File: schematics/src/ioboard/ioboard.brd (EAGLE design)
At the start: 160 x 98.7 mm, 31 parts

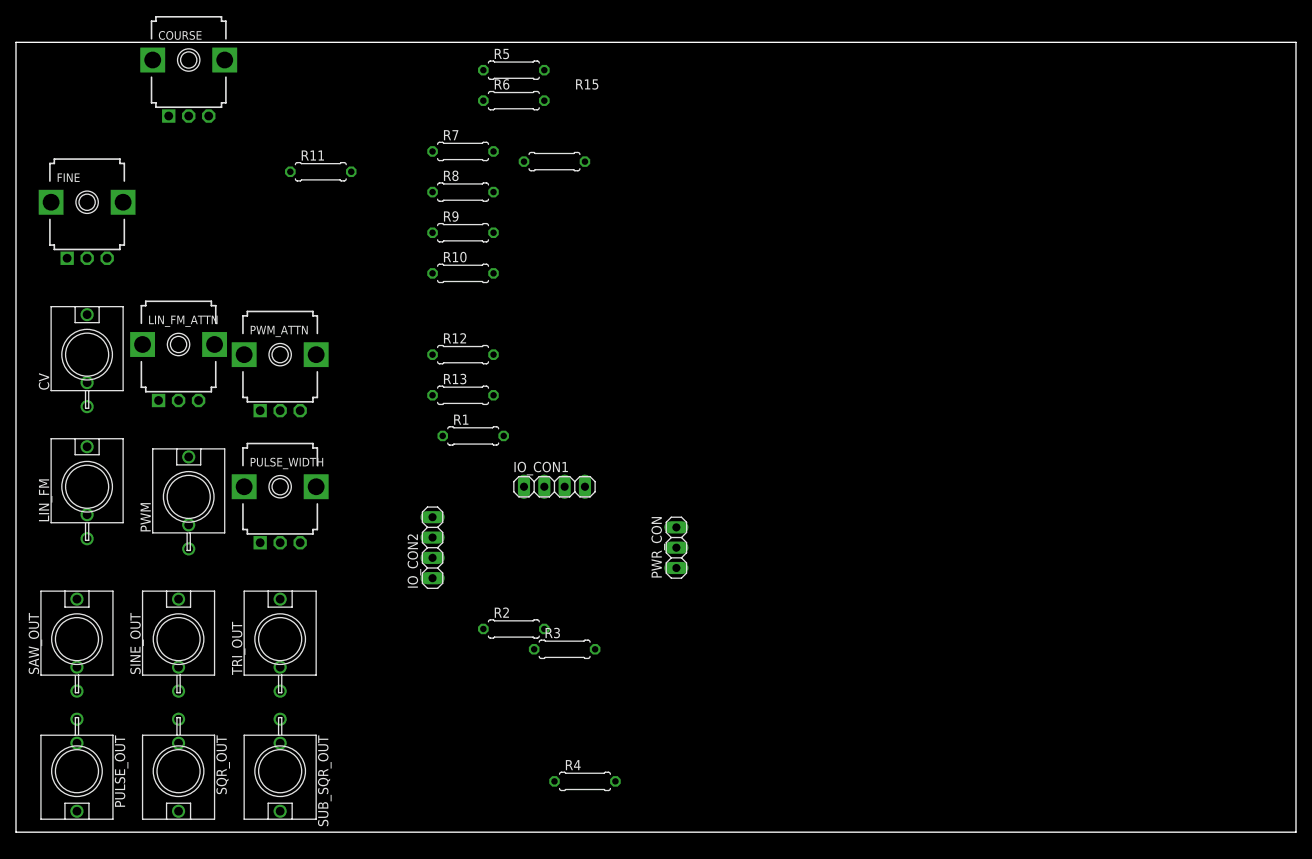
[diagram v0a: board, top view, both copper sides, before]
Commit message: Updated Schematics, Fixed Power Socket orientation
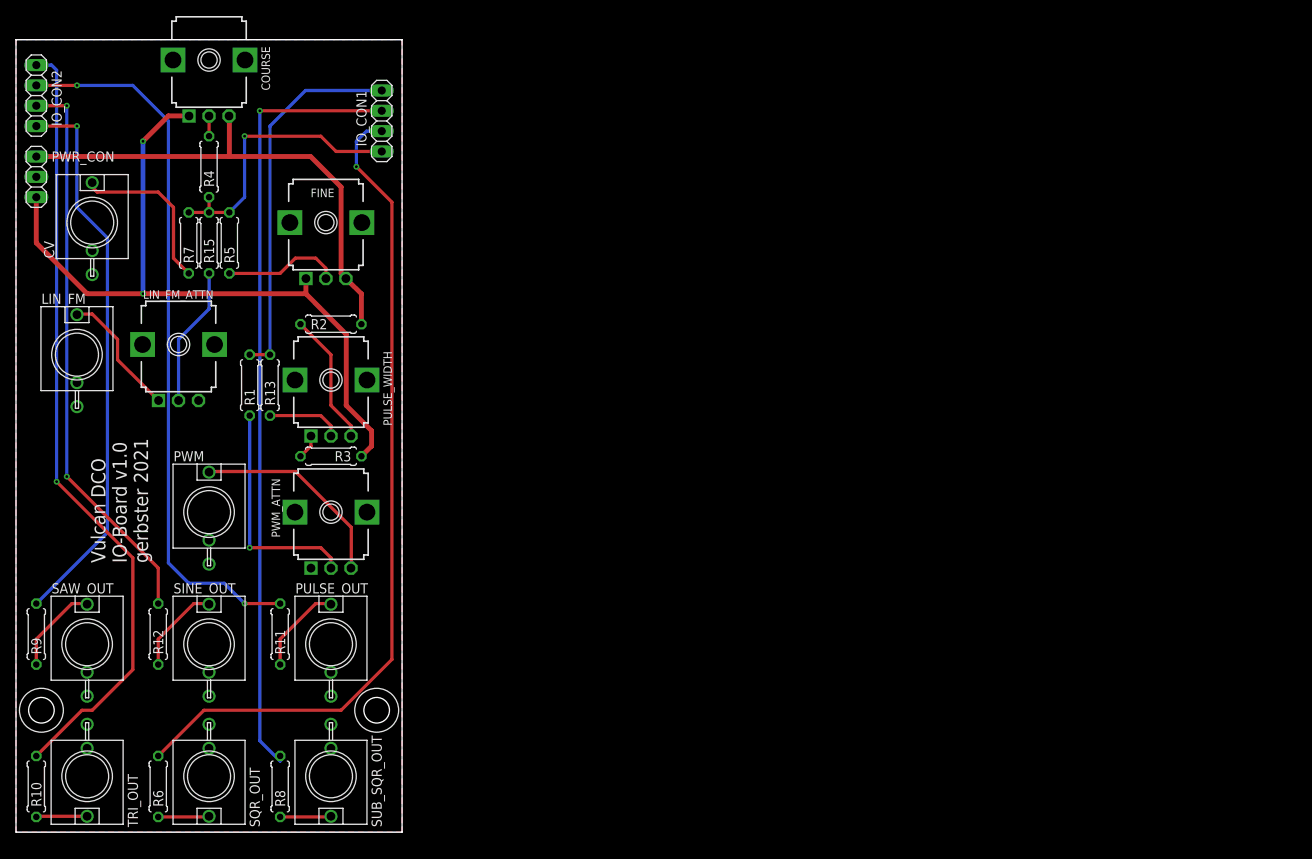
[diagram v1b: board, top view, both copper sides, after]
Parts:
- moved R6 96.6 mm to (17.8, 5.71), turned to 270 degrees
- moved PWR_CON 92.5 mm to (2.54, 81.9)
- moved R4 90.1 mm to (24.1, 83.2), turned to 270 degrees
- moved R10 83.4 mm to (2.54, 5.71), turned to 270 degrees
- moved R8 77.7 mm to (33.0, 5.71), turned to 270 degrees
- moved IO_CON2 75.1 mm to (2.54, 92.1)
- moved R9 73.2 mm to (2.54, 24.8), turned to 270 degrees
- moved R11 58.0 mm to (33.0, 24.8), turned to 270 degrees
- moved R12 51.7 mm to (17.8, 24.8), turned to 270 degrees
- moved IO_CON1 50.6 mm to (45.7, 88.9), turned to 270 degrees
- moved R2 44.4 mm to (39.4, 63.5)
- moved R15 44.4 mm to (24.1, 73.7), turned to 90 degrees
- moved R5 41.6 mm to (26.7, 73.7), turned to 90 degrees
- moved R3 37.9 mm to (39.4, 47.0), turned to 180 degrees
- moved R7 36.1 mm to (21.6, 73.7), turned to 90 degrees
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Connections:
- net CV_INPUT: now also IO_CON1.4; no longer IO_CON1.2
- net PULSE_OUT: now also IO_CON2.3; no longer IO_CON2.4
- net SAW_OUT: now also IO_CON2.1; no longer IO_CON2.2
- net SINE_OUT: now also IO_CON2.2; no longer IO_CON2.3
- net SQR_OUT: now also IO_CON1.3; no longer IO_CON1.4
- net SUB_SQR_OUT: now also IO_CON1.2; no longer IO_CON1.3
- net TRI_OUT: now also IO_CON2.4; no longer IO_CON2.1
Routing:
- net SQR_OUT: track 0.00 -> 104.5 mm, vias 0 -> 1
- net TRI_OUT: track 0.00 -> 98.2 mm, vias 0 -> 1
- net SUB_SQR_OUT: track 0.00 -> 98.2 mm, vias 0 -> 1
- net -12V: track 0.00 -> 94.3 mm, vias 0 -> 2
- net PULSE_OUT: track 0.00 -> 89.7 mm, vias 0 -> 2
- net SINE_OUT: track 0.00 -> 70.8 mm, vias 0 -> 2
- net SAW_OUT: track 0.00 -> 70.0 mm, vias 0 -> 1
- net +12V: track 0.00 -> 63.0 mm
- net PWM_SET: track 0.00 -> 46.9 mm
- net CV_INPUT: track 0.00 -> 35.2 mm, vias 0 -> 1
- net N$14: track 0.00 -> 28.5 mm, vias 0 -> 1
- net N$12: track 0.00 -> 25.9 mm
- net N$4: track 0.00 -> 20.8 mm
- net N$44: track 0.00 -> 17.5 mm
- net N$3: track 0.00 -> 16.6 mm
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- added copper zone on layer 1, net GND
- added copper zone on layer 16, net GND
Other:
- board size 160 x 98.7 mm -> 48.3 x 99.1 mm
- board text added: "Vulcan DCO IO-Board v1.0 gerbster 2021"
